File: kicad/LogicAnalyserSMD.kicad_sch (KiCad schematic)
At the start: 318 parts, among them J1 AgilentPod40, J2 AgilentPod40, J3 AgilentPod40, J4 AgilentPod40, J5 AgilentPod40, J6 AgilentPod40, J7 Conn_01x05_Pin, J8 Conn_01x02_Pin, P1 S100_MALE_A, P34 CONN_1, P35 CONN_1, U1 74LS00

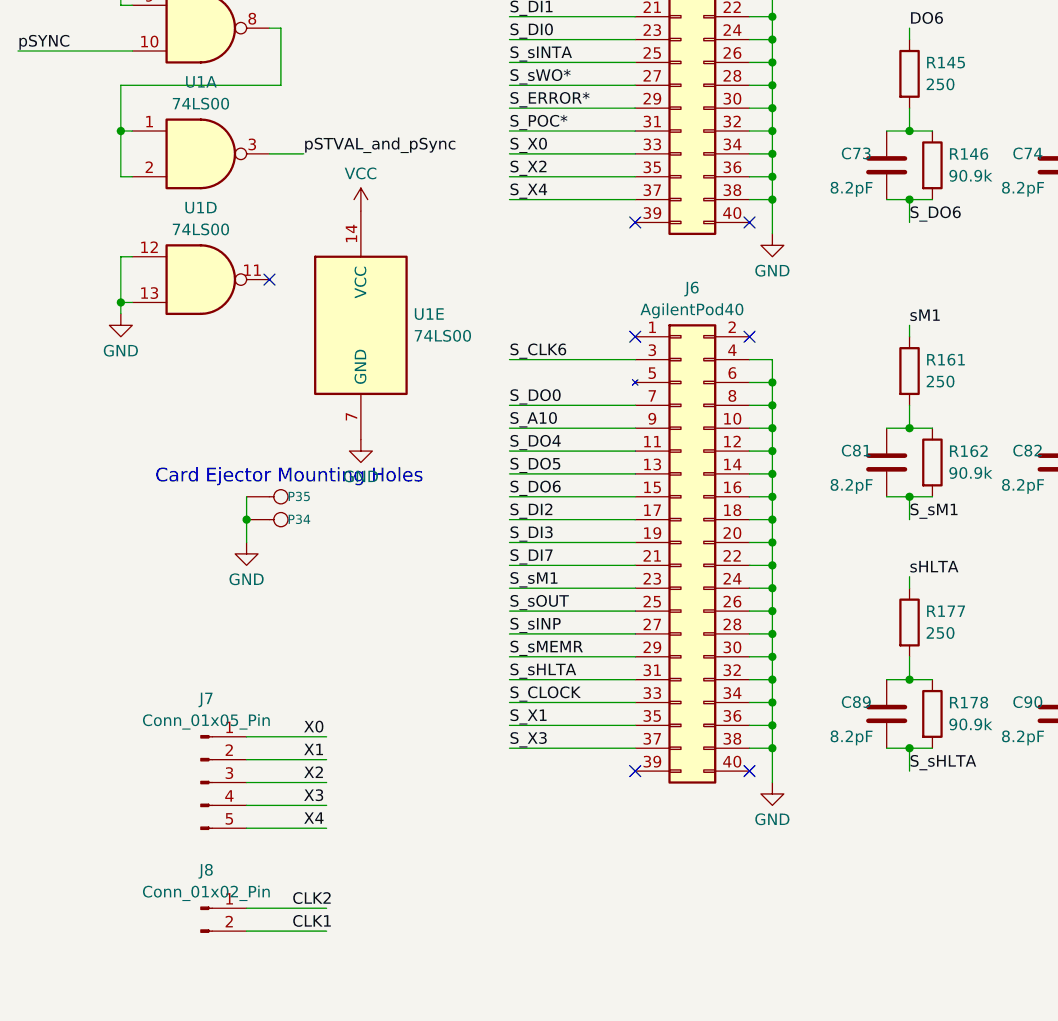
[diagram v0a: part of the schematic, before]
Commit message: Add bypass capacitor and adjust track widths
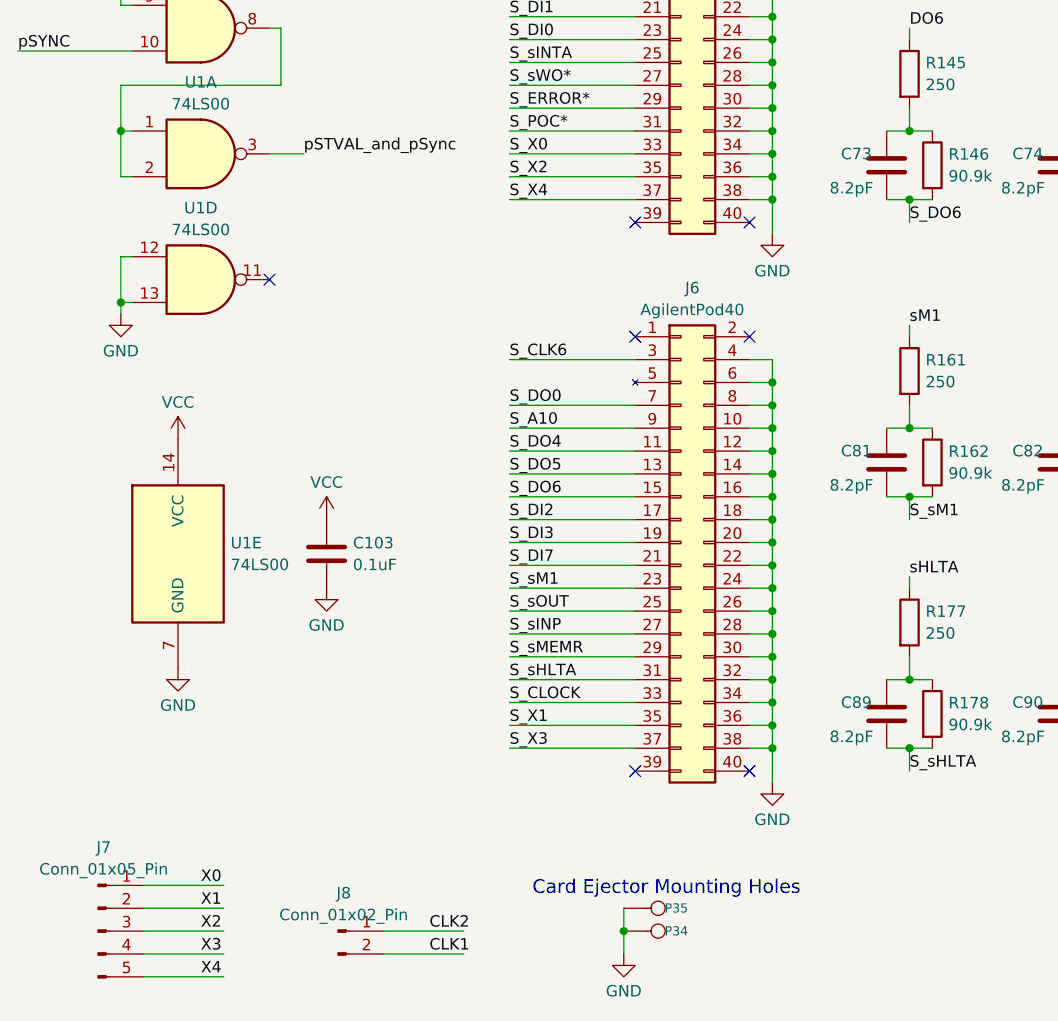
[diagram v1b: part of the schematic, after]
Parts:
- added C103: 0.1uF, Capacitor_SMD:C_0805_2012Metric, symbol Device:C
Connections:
- net GND: now also C103.2
- net VCC: now also C103.1
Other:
- moved on the sheet: J7, J8, P34, P35, U1E
